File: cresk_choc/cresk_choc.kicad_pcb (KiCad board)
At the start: 2 copper layers, 102 x 73 mm, 21 parts, among them J1 TRRS, J2 BATTERY, SW1 SW_Push, SW10 SW_Push, SW11 SW_Push, SW12 SW_Push, SW13 SW_Push, SW14 SW_Push, SW15 SW_Push, SW16 SW_Push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

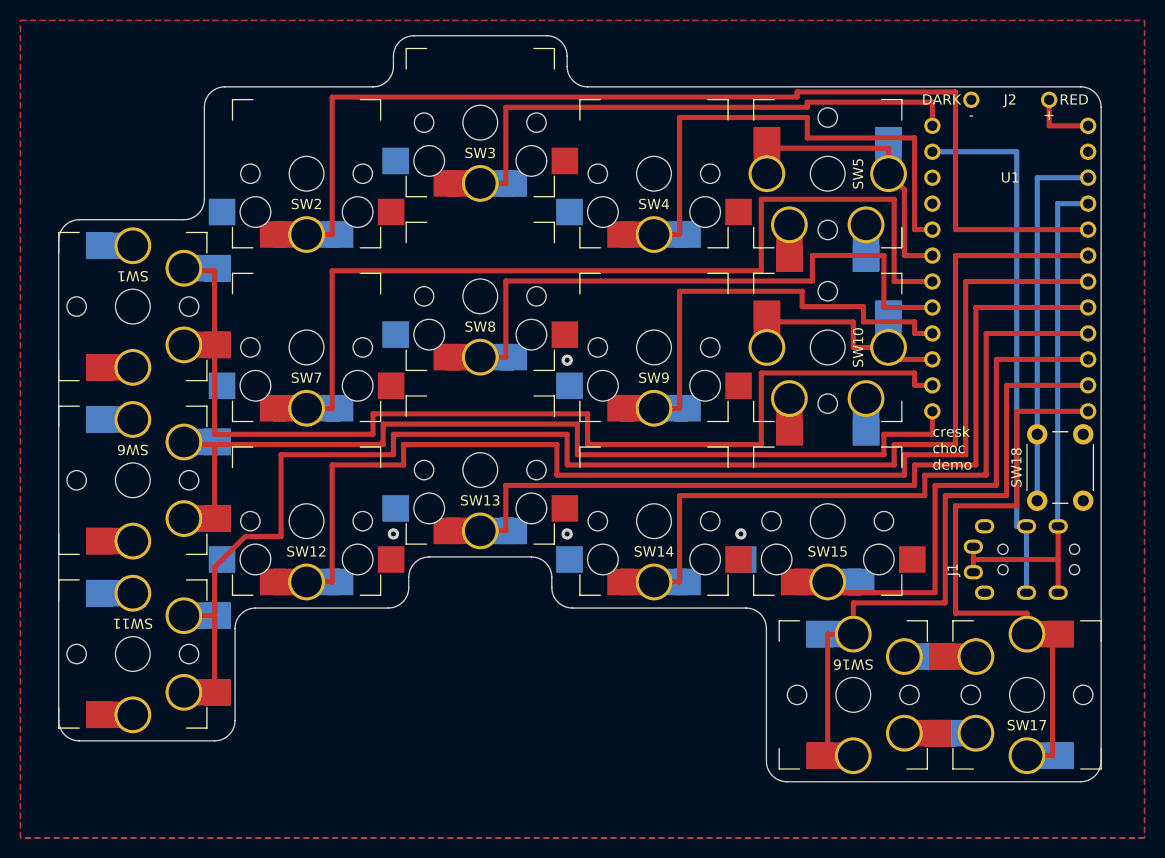
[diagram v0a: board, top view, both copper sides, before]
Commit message: cresk_choc: test drill sizes
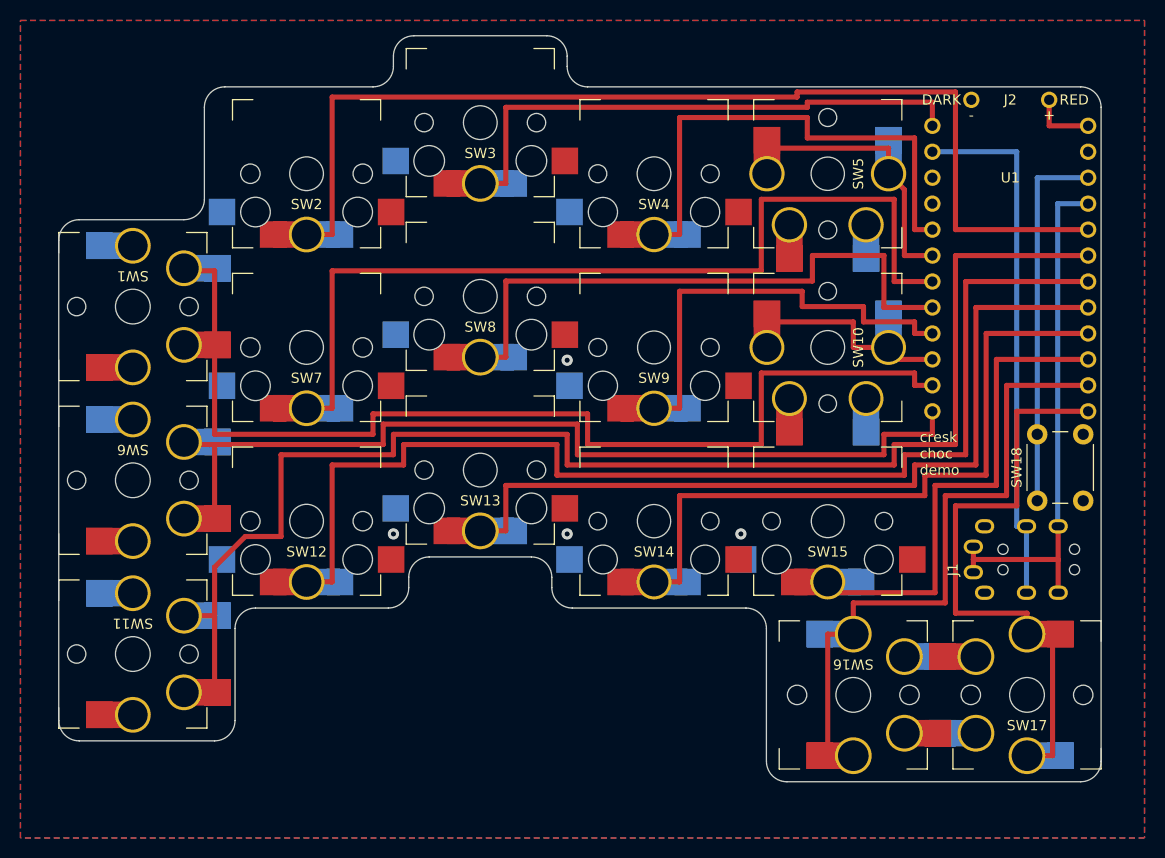
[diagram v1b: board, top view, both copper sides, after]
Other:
- board text added: "Center pin 3.3mm Fixing pin 1.8mm Socket 3.0mm (spec) SW3 SW8 SW13"
- board text added: "Center pin 3.3mm Socket 2.9mm SW2 SW7 SW12"
- board text added: "Fixing pin 1.76mm Socket 2.86mm Center pin 3.3mm 3.26mm 3.22mm SW4 SW5 SW9"
- board text added: "Fixing pins 1.72mm Socket 2.82mm Center pin 3.3mm 3.26mm 3.22mm SW10 SW14 SW15"
- board text added: "Fixing pins 1.8mm"
- board text added: "Padded socket 2.9mm"
- board text added: "SW1 SW6 SW11"
